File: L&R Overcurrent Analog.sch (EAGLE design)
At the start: 17 parts, among them IC1 CSLA2CFTH, IC2 TLC393CPN, Q1 SUP75P0307, Q2 SUP75P0307, X1 J1

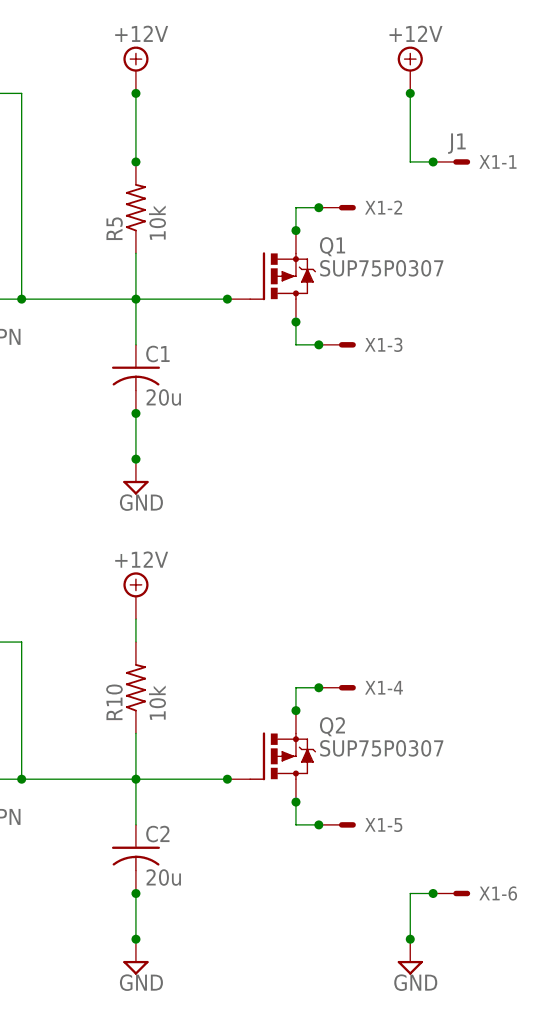
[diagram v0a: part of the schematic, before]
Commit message: Moved current transducer closer on board, larger ground pour.
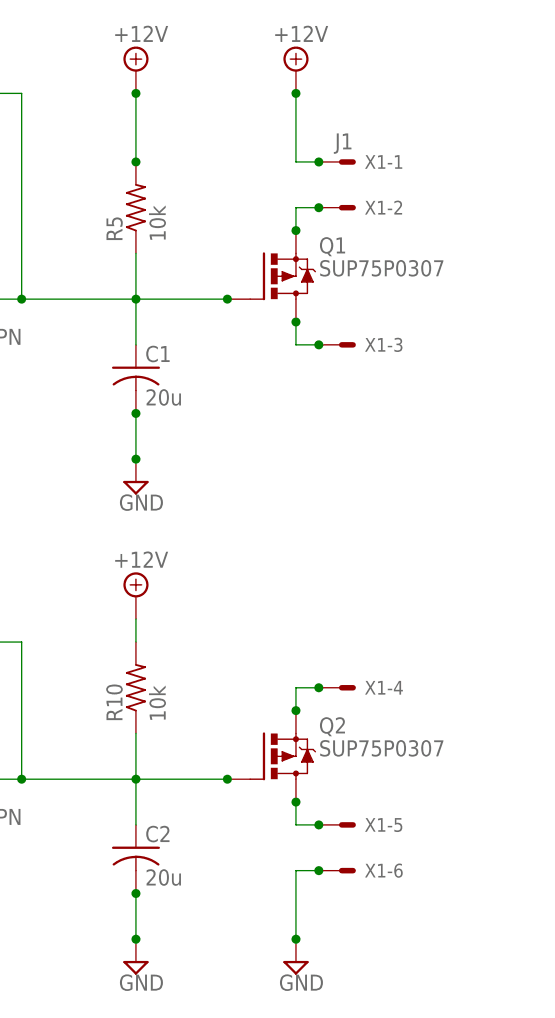
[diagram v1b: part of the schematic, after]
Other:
- moved on the sheet: X1-1, X1-6
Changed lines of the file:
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@@
 <instance part="C1" gate="G$1" x="27.94" y="17.78"/>
 <instance part="C2" gate="G$1" x="27.94" y="-35.56"/>
-<instance part="X1" gate="-1" x="63.5" y="40.64"/>
+<instance part="X1" gate="-1" x="50.8" y="40.64"/>
 <instance part="X1" gate="-2" x="50.8" y="35.56"/>
 <instance part="X1" gate="-3" x="50.8" y="20.32"/>
 <instance part="X1" gate="-4" x="50.8" y="-17.78"/>
 <instance part="X1" gate="-5" x="50.8" y="-33.02"/>
-<instance part="X1" gate="-6" x="63.5" y="-40.64"/>
+<instance part="X1" gate="-6" x="50.8" y="-38.1"/>
 <instance part="SUPPLY1" gate="GND" x="-45.72" y="15.24"/>
 <instance part="SUPPLY2" gate="+12V" x="-45.72" y="50.8"/>
@@
 <instance part="SUPPLY9" gate="GND" x="27.94" y="5.08"/>
 <instance part="SUPPLY10" gate="GND" x="27.94" y="-48.26"/>
-<instance part="SUPPLY11" gate="+12V" x="58.42" y="50.8"/>
-<instance part="SUPPLY12" gate="GND" x="58.42" y="-48.26"/>
+<instance part="SUPPLY11" gate="+12V" x="45.72" y="50.8"/>
+<instance part="SUPPLY12" gate="GND" x="45.72" y="-48.26"/>
 <instance part="IC2" gate="P" x="0" y="25.4"/>
 <instance part="SUPPLY13" gate="+12V" x="0" y="38.1"/>
@@
 <segment>
 <pinref part="SUPPLY11" gate="+12V" pin="+12V"/>
-<wire x1="58.42" y1="48.26" x2="58.42" y2="40.64" width="0.1524" layer="91"/>
+<wire x1="45.72" y1="48.26" x2="45.72" y2="40.64" width="0.1524" layer="91"/>
 <pinref part="X1" gate="-1" pin="S"/>
-<wire x1="58.42" y1="40.64" x2="60.96" y2="40.64" width="0.1524" layer="91"/>
-<junction x="58.42" y="48.26"/>
-<junction x="60.96" y="40.64"/>
+<wire x1="45.72" y1="40.64" x2="48.26" y2="40.64" width="0.1524" layer="91"/>
+<junction x="45.72" y="48.26"/>
+<junction x="48.26" y="40.64"/>
 </segment>
 <segment>
@@
 <pinref part="X1" gate="-6" pin="S"/>
 <pinref part="SUPPLY12" gate="GND" pin="GND"/>
-<wire x1="60.96" y1="-40.64" x2="58.42" y2="-40.64" width="0.1524" layer="91"/>
-<wire x1="58.42" y1="-40.64" x2="58.42" y2="-45.72" width="0.1524" layer="91"/>
-<junction x="60.96" y="-40.64"/>
-<junction x="58.42" y="-45.72"/>
+<wire x1="48.26" y1="-38.1" x2="45.72" y2="-38.1" width="0.1524" layer="91"/>
+<wire x1="45.72" y1="-38.1" x2="45.72" y2="-45.72" width="0.1524" layer="91"/>
+<junction x="48.26" y="-38.1"/>
+<junction x="45.72" y="-45.72"/>
 </segment>
 <segment>

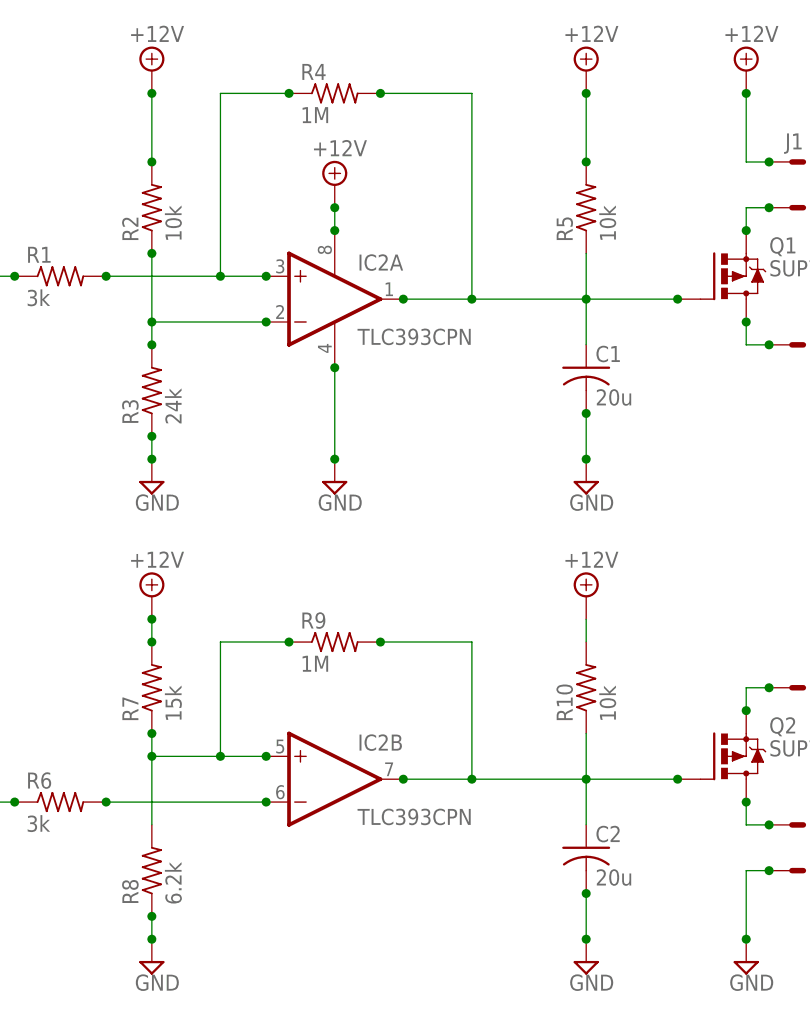
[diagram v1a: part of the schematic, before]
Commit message: Added IC filter cap, changed RC timer caps to electrolytic.
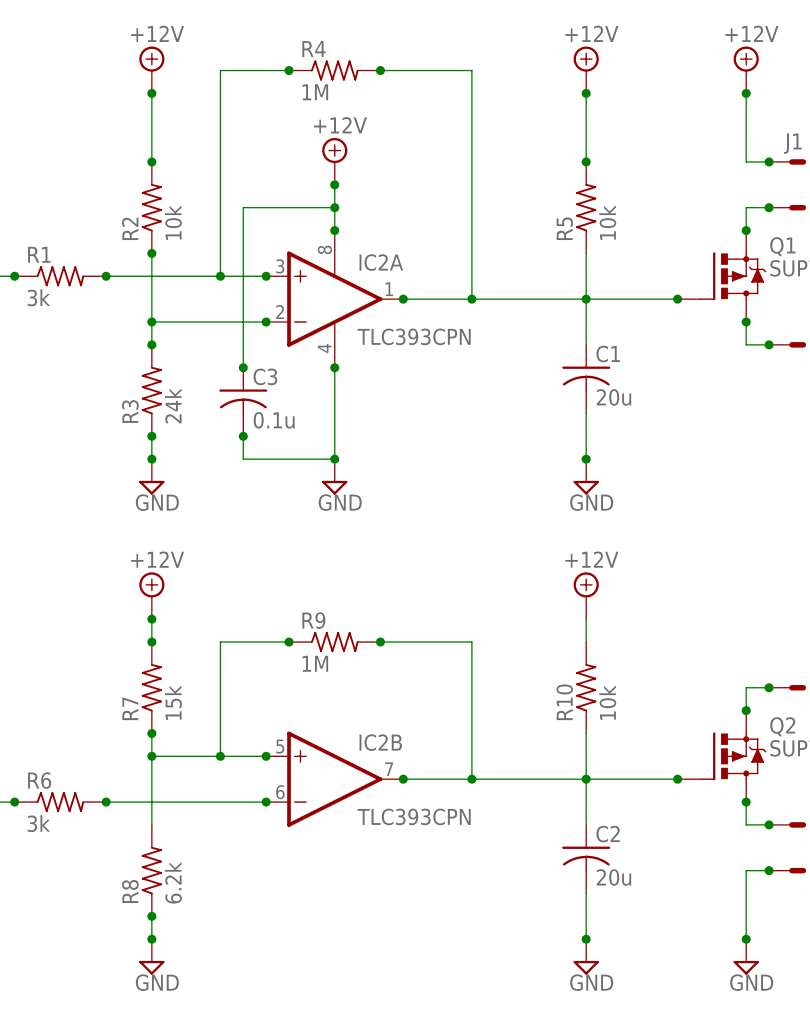
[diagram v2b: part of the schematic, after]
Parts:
- added C3: 0.1u, Overcurrent Detect:CAPACITOR-US
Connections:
- net +12V: now also C3.1
- net GND: now also C3.2
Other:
- moved on the sheet: R4
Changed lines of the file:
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@@
 <part name="Q1" library="Overcurrent Detect" deviceset="SUP75P03" device="07"/>
 <part name="Q2" library="Overcurrent Detect" deviceset="SUP75P03" device="07"/>
-<part name="C1" library="Overcurrent Detect" deviceset="CAPACITOR-US" device="025-050X050" value="20u"/>
-<part name="C2" library="Overcurrent Detect" deviceset="CAPACITOR-US" device="025-050X050" value="20u"/>
 <part name="X1" library="Overcurrent Detect" deviceset="6PIN_HEADER" device="" value="J1"/>
 <part name="SUPPLY1" library="Overcurrent Detect" deviceset="GND" device=""/>
@@
 <part name="SUPPLY13" library="Overcurrent Detect" deviceset="+12V" device=""/>
 <part name="SUPPLY14" library="Overcurrent Detect" deviceset="GND" device=""/>
+<part name="C1" library="Overcurrent Detect" deviceset="CAPACITOR-US" device="025-050X050" value="20u"/>
+<part name="C2" library="Overcurrent Detect" deviceset="CAPACITOR-US" device="025-050X050" value="20u"/>
+<part name="C3" library="Overcurrent Detect" deviceset="CAPACITOR-US" device="" value="0.1u"/>
 </parts>
 <sheets>
@@
 <instance part="R2" gate="G$1" x="-20.32" y="35.56" rot="R90"/>
 <instance part="R3" gate="G$1" x="-20.32" y="15.24" rot="R90"/>
-<instance part="R4" gate="G$1" x="0" y="48.26"/>
+<instance part="R4" gate="G$1" x="0" y="50.8"/>
 <instance part="R5" gate="G$1" x="27.94" y="35.56" rot="R90"/>
 <instance part="R6" gate="G$1" x="-30.48" y="-30.48"/>
@@
 <instance part="Q1" gate="G$1" x="43.18" y="27.94"/>
 <instance part="Q2" gate="G$1" x="43.18" y="-25.4"/>
-<instance part="C1" gate="G$1" x="27.94" y="17.78"/>
-<instance part="C2" gate="G$1" x="27.94" y="-35.56"/>
 <instance part="X1" gate="-1" x="50.8" y="40.64"/>
 <instance part="X1" gate="-2" x="50.8" y="35.56"/>
@@
 <instance part="SUPPLY12" gate="GND" x="45.72" y="-48.26"/>
 <instance part="IC2" gate="P" x="0" y="25.4"/>
-<instance part="SUPPLY13" gate="+12V" x="0" y="38.1"/>
+<instance part="SUPPLY13" gate="+12V" x="0" y="40.64"/>
 <instance part="SUPPLY14" gate="GND" x="0" y="5.08"/>
+<instance part="C1" gate="G$1" x="27.94" y="17.78"/>
+<instance part="C2" gate="G$1" x="27.94" y="-35.56"/>
+<instance part="C3" gate="G$1" x="-10.16" y="15.24"/>
 </instances>
 <busses>
@@
 <pinref part="SUPPLY13" gate="+12V" pin="+12V"/>
 <wire x1="0" y1="33.02" x2="0" y2="35.56" width="0.1524" layer="91"/>
+<junction x="0" y="38.1"/>
+<junction x="0" y="33.02"/>
+<pinref part="C3" gate="G$1" pin="1"/>
+<wire x1="0" y1="35.56" x2="0" y2="38.1" width="0.1524" layer="91"/>
+<wire x1="-10.16" y1="17.78" x2="-10.16" y2="35.56" width="0.1524" layer="91"/>
+<wire x1="-10.16" y1="35.56" x2="0" y2="35.56" width="0.1524" layer="91"/>
+<junction x="-10.16" y="17.78"/>
 <junction x="0" y="35.56"/>
-<junction x="0" y="33.02"/>
 </segment>
 </net>
@@
 </segment>
 <segment>
-<pinref part="C2" gate="G$1" pin="2"/>
 <pinref part="SUPPLY10" gate="GND" pin="GND"/>
 <wire x1="27.94" y1="-40.64" x2="27.94" y2="-45.72" width="0.1524" layer="91"/>
 <junction x="27.94" y="-45.72"/>
-<junction x="27.94" y="-40.64"/>
-</segment>
-<segment>
-<pinref part="C1" gate="G$1" pin="2"/>
+<pinref part="C2" gate="G$1" pin="2"/>
+</segment>
+<segment>
 <pinref part="SUPPLY9" gate="GND" pin="GND"/>
 <wire x1="27.94" y1="12.7" x2="27.94" y2="7.62" width="0.1524" layer="91"/>
-<junction x="27.94" y="12.7"/>
 <junction x="27.94" y="7.62"/>
+<pinref part="C1" gate="G$1" pin="2"/>
 </segment>
 <segment>
@@
 <junction x="0" y="17.78"/>
 <junction x="0" y="7.62"/>
+<pinref part="C3" gate="G$1" pin="2"/>
+<wire x1="-10.16" y1="10.16" x2="-10.16" y2="7.62" width="0.1524" layer="91"/>
+<wire x1="-10.16" y1="7.62" x2="0" y2="7.62" width="0.1524" layer="91"/>
+<junction x="-10.16" y="10.16"/>
 </segment>
 </net>
@@
 <pinref part="R4" gate="G$1" pin="1"/>
 <wire x1="-12.7" y1="27.94" x2="-7.62" y2="27.94" width="0.1524" layer="91"/>
-<wire x1="-5.08" y1="48.26" x2="-12.7" y2="48.26" width="0.1524" layer="91"/>
-<wire x1="-12.7" y1="48.26" x2="-12.7" y2="27.94" width="0.1524" layer="91"/>
+<wire x1="-5.08" y1="50.8" x2="-12.7" y2="50.8" width="0.1524" layer="91"/>
+<wire x1="-12.7" y1="50.8" x2="-12.7" y2="27.94" width="0.1524" layer="91"/>
 <junction x="-25.4" y="27.94"/>
 <junction x="-7.62" y="27.94"/>
 <junction x="-12.7" y="27.94"/>
-<junction x="-5.08" y="48.26"/>
+<junction x="-5.08" y="50.8"/>
 </segment>
 </net>
@@
 <segment>
 <pinref part="R4" gate="G$1" pin="2"/>
-<wire x1="5.08" y1="48.26" x2="15.24" y2="48.26" width="0.1524" layer="91"/>
-<wire x1="15.24" y1="48.26" x2="15.24" y2="25.4" width="0.1524" layer="91"/>
+<wire x1="5.08" y1="50.8" x2="15.24" y2="50.8" width="0.1524" layer="91"/>
+<wire x1="15.24" y1="50.8" x2="15.24" y2="25.4" width="0.1524" layer="91"/>
 <pinref part="IC2" gate="A" pin="OUT"/>
 <wire x1="15.24" y1="25.4" x2="7.62" y2="25.4" width="0.1524" layer="91"/>
-<junction x="5.08" y="48.26"/>
+<junction x="5.08" y="50.8"/>
 <junction x="7.62" y="25.4"/>
 <pinref part="Q1" gate="G$1" pin="G"/>
@@
 <junction x="15.24" y="25.4"/>
 <pinref part="R5" gate="G$1" pin="1"/>
-<pinref part="C1" gate="G$1" pin="1"/>
 <wire x1="27.94" y1="25.4" x2="38.1" y2="25.4" width="0.1524" layer="91"/>
 <wire x1="27.94" y1="30.48" x2="27.94" y2="25.4" width="0.1524" layer="91"/>
@@
 <wire x1="27.94" y1="25.4" x2="27.94" y2="20.32" width="0.1524" layer="91"/>
 <junction x="38.1" y="25.4"/>
+<pinref part="C1" gate="G$1" pin="1"/>
 </segment>
 </net>
@@
 <junction x="15.24" y="-27.94"/>
 <pinref part="R10" gate="G$1" pin="1"/>
-<pinref part="C2" gate="G$1" pin="1"/>
 <wire x1="27.94" y1="-27.94" x2="38.1" y2="-27.94" width="0.1524" layer="91"/>
 <wire x1="27.94" y1="-22.86" x2="27.94" y2="-27.94" width="0.1524" layer="91"/>
@@
 <wire x1="27.94" y1="-27.94" x2="27.94" y2="-33.02" width="0.1524" layer="91"/>
 <junction x="38.1" y="-27.94"/>
-</segment>
-</net>
+<pinref part="C2" gate="G$1" pin="1"/>
+</segment>
+</net>

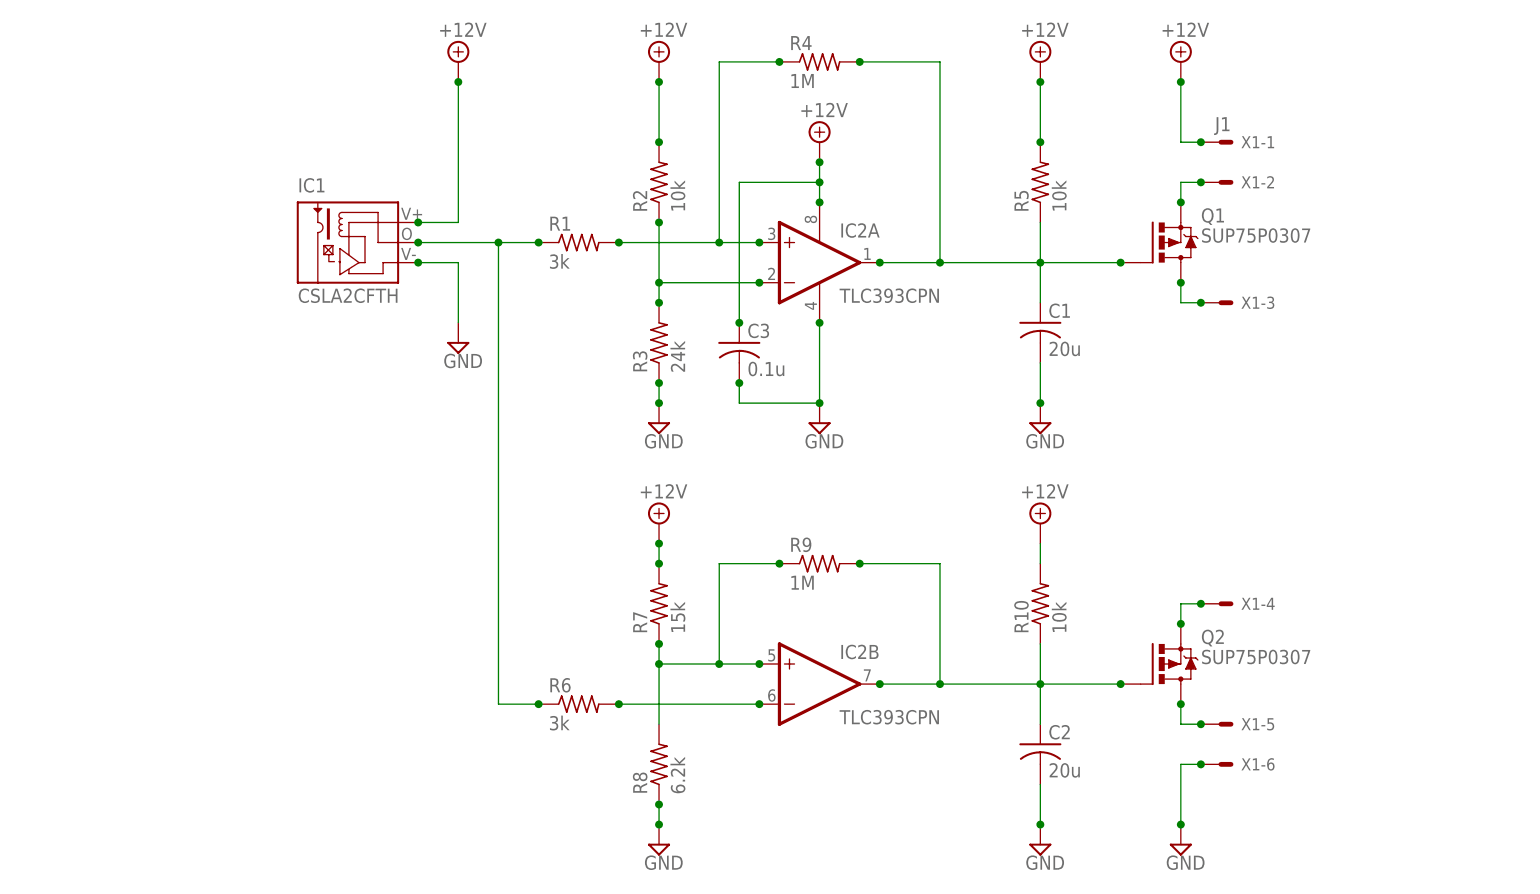
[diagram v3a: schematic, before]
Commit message: Changed to 5V, added regulator. PCB not done.
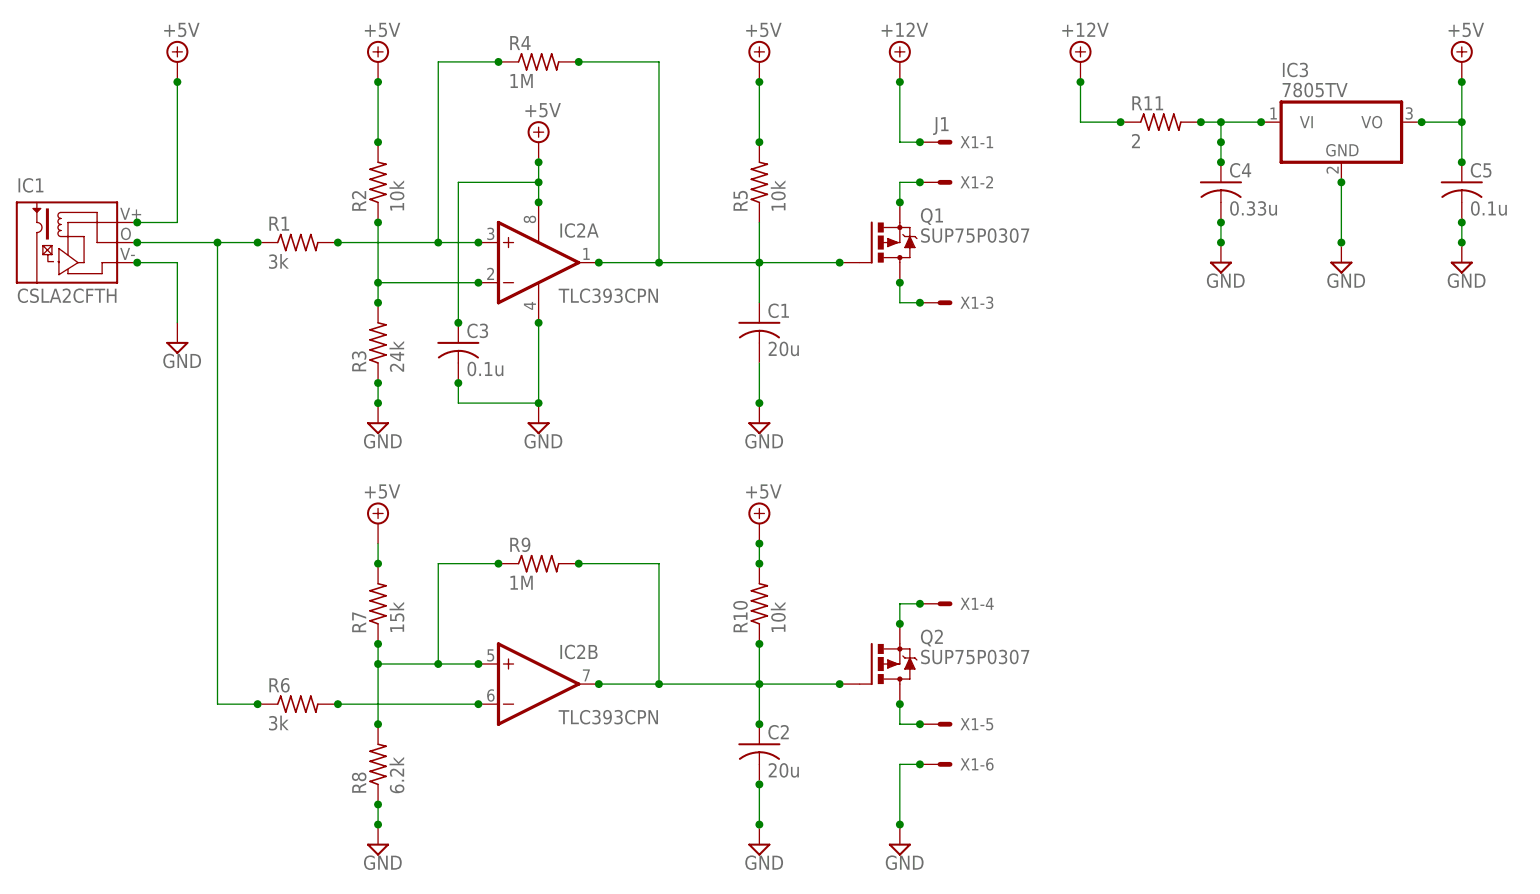
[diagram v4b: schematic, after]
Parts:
- added C4: 0.33u, Overcurrent Detect:CAPACITOR-US
- added C5: 0.1u, Overcurrent Detect:CAPACITOR-US
- added IC3: 7805TV, Overcurrent Detect:7805TV
- added R11: 2, Overcurrent Detect:RESISTOR-US0617/22
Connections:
- new net +5V: C3.1, C5.1, IC1.V+, IC2P.V+, IC3.VO, R10.2, R2.2, R5.2, R7.2
- new net N$12: C4.1, IC3.VI, R11.2
- net +12V: now also R11.1; no longer C3.1, IC1.V+, IC2P.V+, R10.2, R2.2, R5.2, R7.2
- net GND: now also C4.2, C5.2, IC3.GND
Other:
- moved on the sheet: C1, C2, C3, IC1, IC2A, IC2B, Q1, Q2, R1, R10, R2, R3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
